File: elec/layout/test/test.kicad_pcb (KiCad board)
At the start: 2 copper layers, 8 parts, among them U3 10µH ±20%

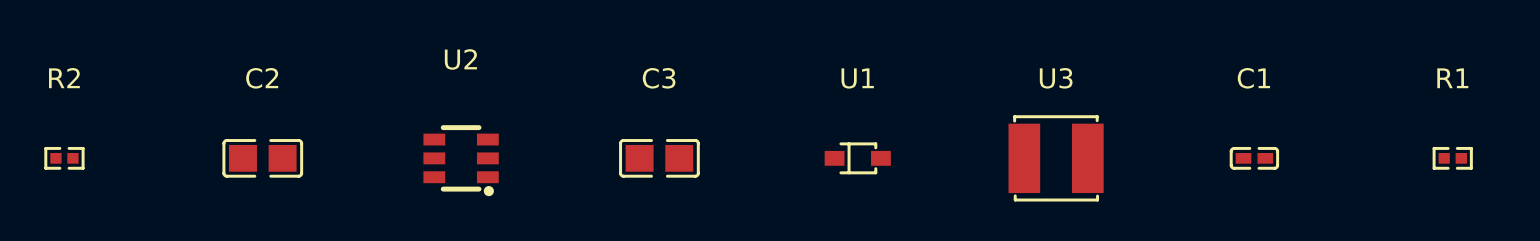
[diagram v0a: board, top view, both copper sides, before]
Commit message: failing post pick verification
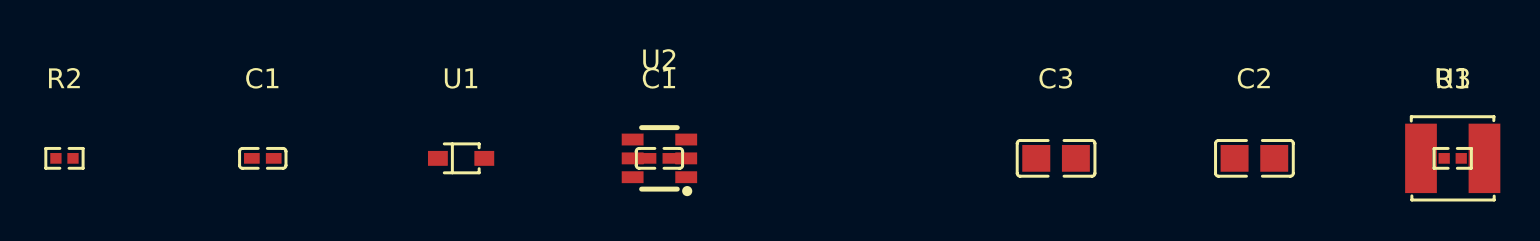
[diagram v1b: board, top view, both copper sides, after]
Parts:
- removed the C1 at (70.0, -5.00)
- added C1: 1µF ±10% 25V X5R, atopile:C0402-b3ef17, F.Cu at (40.0, -5.00)
- added C1: 470nF ±20% 16V X5R, atopile:C0402-b3ef17, F.Cu at (20.0, -5.00)
- C2: value 4.7µF ±10% 25V X5R -> 10µF ±10% 25V X5R
- R1: value 11kΩ ±1% 62.5mW -> 7.5kΩ ±1% 62.5mW
- R2: value 100kΩ ±1% 62.5mW -> 24kΩ ±1% 62.5mW
- moved C2 50.0 mm to (70.0, -5.00)
- moved C3 20.0 mm to (60.0, -5.00)
- moved U1 20.0 mm to (30.0, -5.00)
- moved U3 20.0 mm to (80.0, -5.00)
- moved U2 10.0 mm to (40.0, -5.00)
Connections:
- net SW renamed cathode
- C2 pad 1: hv-1 -> hv
- C2 pad 2: gnd-1 -> gnd
- C3 pad 1: hv -> hv-1
- C3 pad 2: gnd -> gnd-1
- R1 pad 2: gnd -> gnd-1
- R2 pad 1: hv -> hv-1
- U1 pad 2: gnd -> gnd-1
- U2 pad 2: gnd-1 -> gnd
- U2 pad 4: hv-1 -> hv
- U2 pad 5: hv-1 -> hv
- U3 pad 2: hv -> hv-1
